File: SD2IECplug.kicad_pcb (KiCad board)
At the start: 2 copper layers, 50 x 49 mm, 39 parts, among them J1 ISP, J2 X6, J4 IEC, J5 C64-CassettePort, J6 C64-CassettePort, J7 Power, J8 X3, Q1 IRLML2803, Q2 IRLML2803, Q3 IRLML2803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

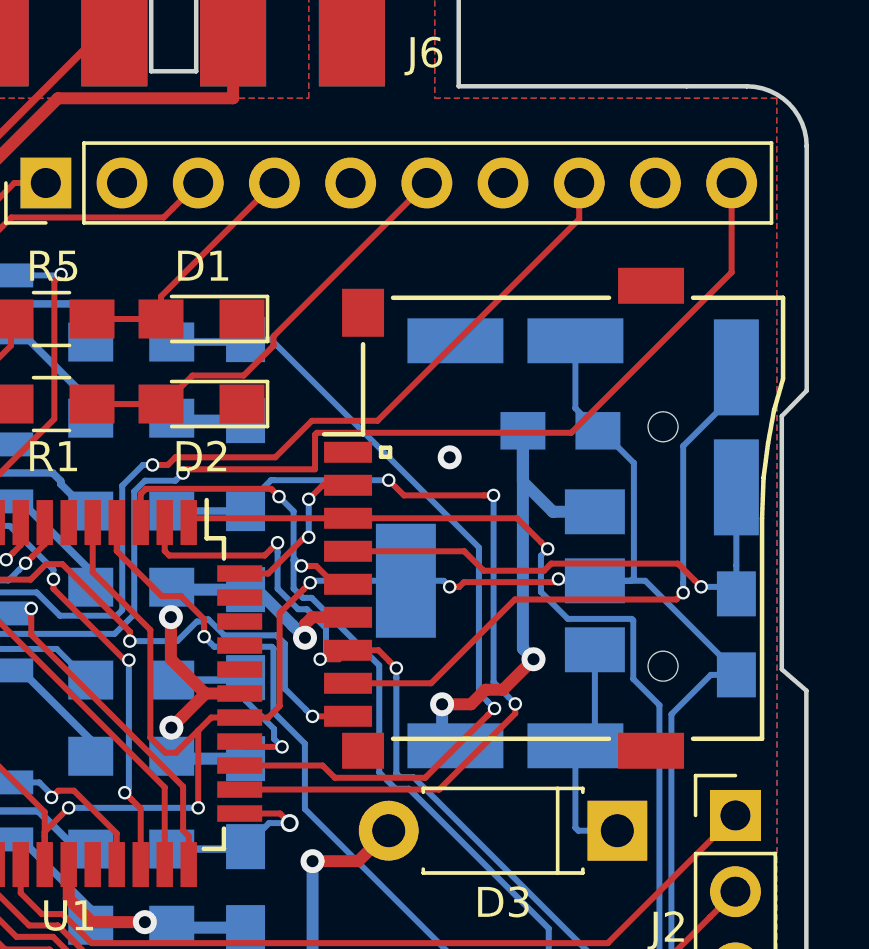
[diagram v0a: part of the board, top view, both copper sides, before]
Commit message: Moced SD connector.
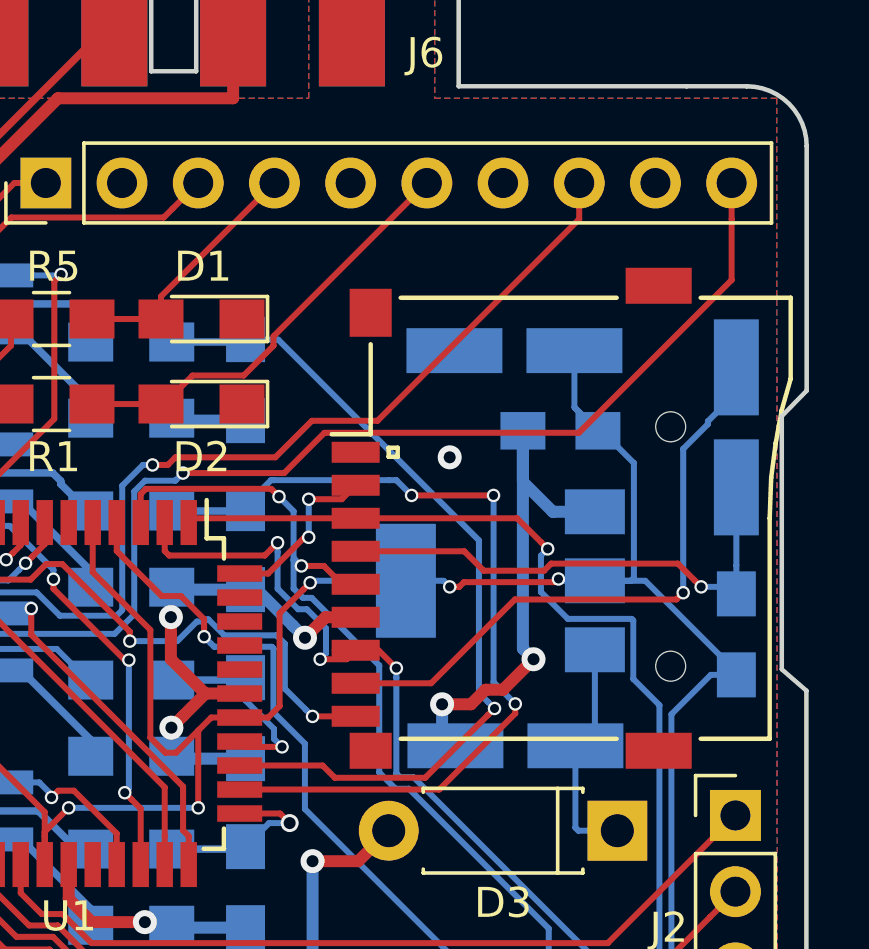
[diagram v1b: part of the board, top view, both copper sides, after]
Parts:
- moved C5 0.33 mm to (98.3, 111.2)
- moved XS1 0.25 mm to (103.5, 116.8)
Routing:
- net +3V3: track 78.6 -> 79.4 mm
- net /IEC_10-11: track 39.0 -> 38.5 mm

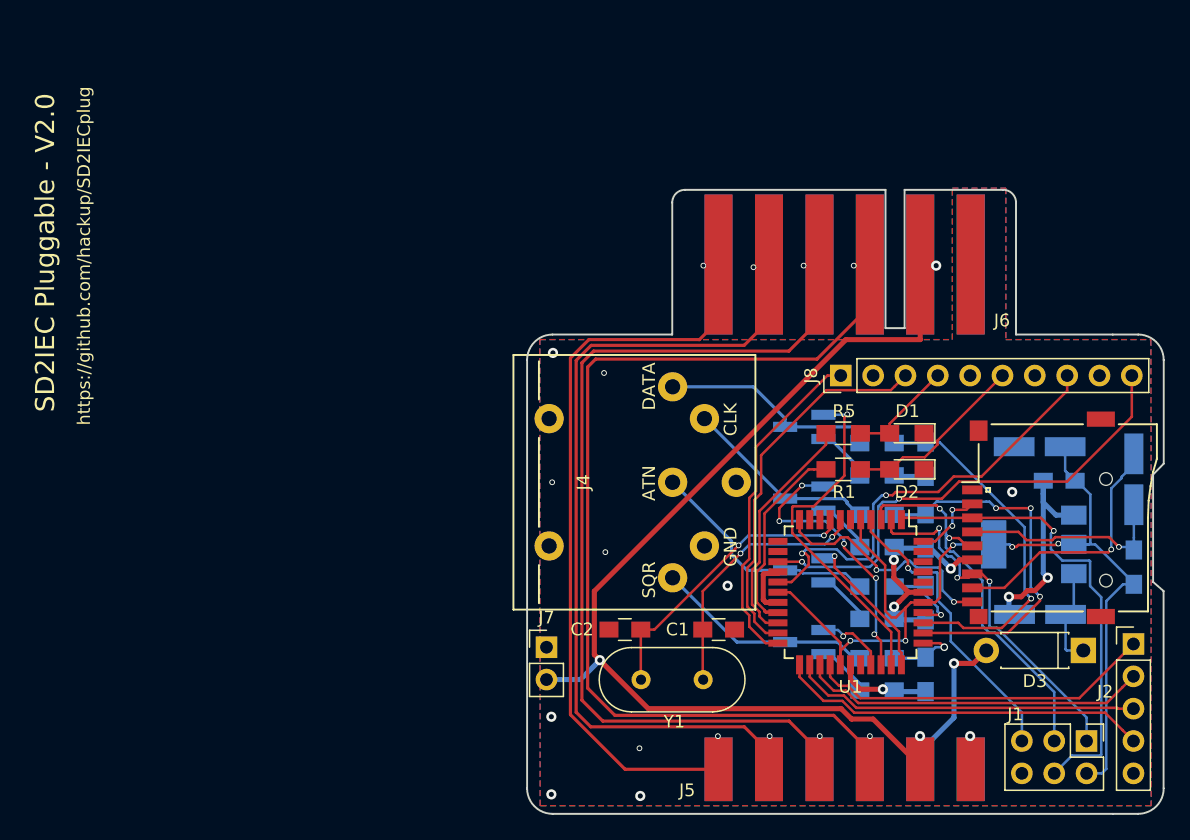
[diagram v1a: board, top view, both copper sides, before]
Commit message: Ziptie holes and silk screen cleanup.
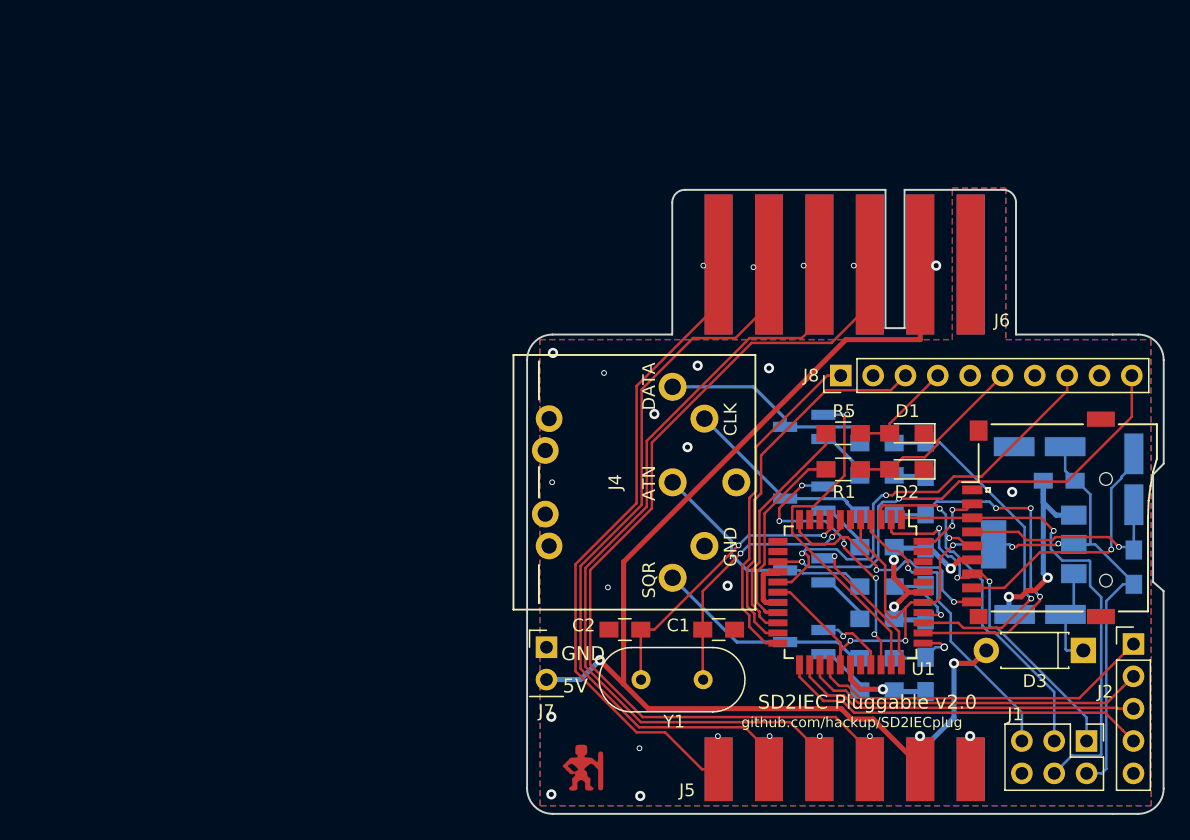
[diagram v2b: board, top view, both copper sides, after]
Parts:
- added G***: LOGO, Logo:bigby2, F.Cu at (62.4, 136.3)
- added MH1: ZipTie, DIN-Connectors:ZipTie_2.7mm, F.Cu at (63.0, 111.6)
- added MH2: ZipTie, DIN-Connectors:ZipTie_2.7mm, F.Cu at (63.0, 116.4)
- J4: footprint DIN-Connectors:DIN-6 -> DIN-Connectors:DIN-6-Variable
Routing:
- net Cas-Read: track 80.4 -> 71.9 mm
- net Cas-Motor: track 86.1 -> 78.2 mm
- net Cas-Sense: track 66.4 -> 58.7 mm
- net Cas-Write: track 74.2 -> 66.6 mm
- net Cas-5V: track 99.1 -> 99.9 mm
- net Cas-GND: vias 17 -> 21
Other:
- board text added: "5V"
- board text added: "SD2IEC Pluggable v2.0"
- board text added: "github.com/hackup/SD2IECplug"
- board text removed: "SD2IEC Pluggable - V2.0"
- board text removed: "https://github.com/hackup/SD2IECplug"

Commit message: Improved routing.
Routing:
- net +3V3: track 79.4 -> 87.6 mm
- net Net-(R7-Pad2): track 28.5 -> 29.0 mm
- net Cas-GND: track 54.6 -> 55.1 mm, vias 21 -> 23

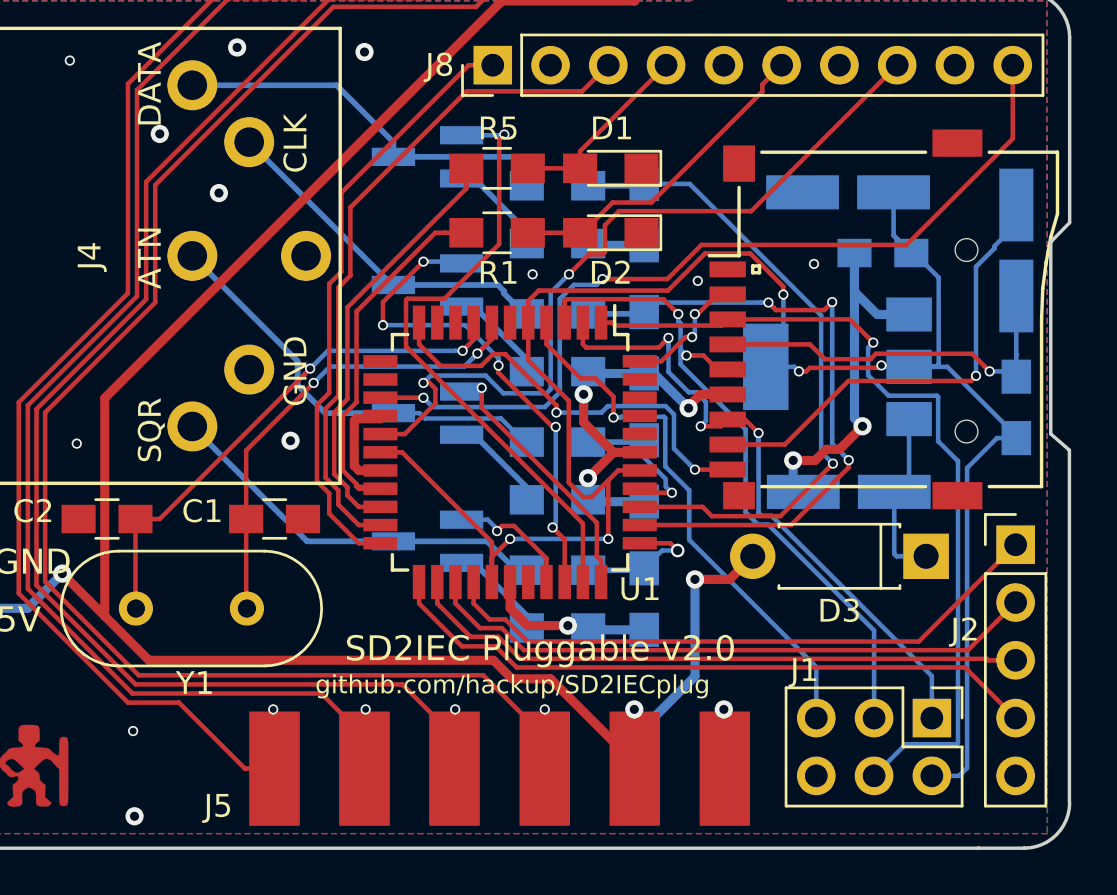
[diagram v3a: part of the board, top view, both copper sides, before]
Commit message: Added missing resistor and yet another breakout header.
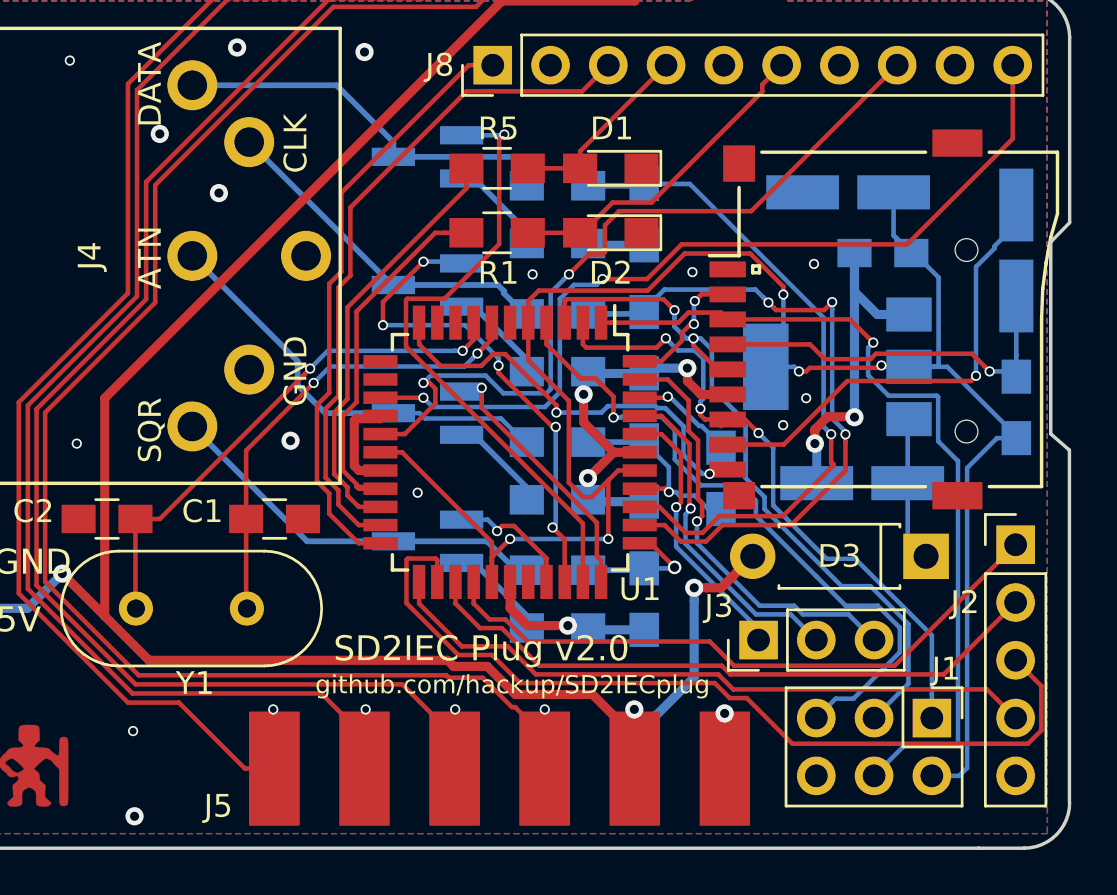
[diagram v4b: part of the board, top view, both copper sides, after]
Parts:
- added J3: Aux, Pin_Headers:Pin_Header_Straight_1x03_Pitch2.54mm, F.Cu at (94.3, 130.9)
- added R16: nB, Resistors_SMD:R_0805_HandSoldering, B.Cu at (92.7, 123.7)
- moved C4 0.70 mm to (98.9, 124.0)
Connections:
- J4 pad 6: (no net) -> Net-(J4-Pad6)
- U1 pad 10: (no net) -> Net-(U1-Pad10)
- U1 pad 12: (no net) -> Net-(U1-Pad12)
- U1 pad 13: (no net) -> Net-(U1-Pad13)
- U1 pad 29: (no net) -> Net-(U1-Pad29)
- U1 pad 40: (no net) -> Net-(J3-Pad1)
- U1 pad 41: (no net) -> Net-(J3-Pad2)
- U1 pad 42: (no net) -> Net-(R16-Pad2)
- U1 pad 43: (no net) -> Net-(J3-Pad3)
- U1 pad 9: (no net) -> Net-(U1-Pad9)
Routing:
- net Net-(J3-Pad3): track 0.00 -> 18.7 mm, vias 0 -> 1
- net Net-(J3-Pad2): track 0.00 -> 14.7 mm, vias 0 -> 1
- net Net-(J3-Pad1): track 0.00 -> 11.9 mm, vias 0 -> 1
- net Net-(J2-Pad3): track 27.4 -> 38.5 mm
- net Net-(J1-Pad5): track 24.0 -> 29.3 mm
- net Net-(R16-Pad2): track 0.00 -> 4.58 mm, vias 0 -> 1
- net Net-(R16-Pad1): track 6.79 -> 9.16 mm
- net SCK: track 30.6 -> 32.5 mm
- net Cas-GND: track 55.1 -> 53.9 mm, vias 23 -> 26
- net Net-(R10-Pad2): track 29.1 -> 30.0 mm
- net Net-(J2-Pad2): track 27.3 -> 28.2 mm
- net Net-(J2-Pad1): track 27.2 -> 28.1 mm
- net Net-(R7-Pad2): track 29.0 -> 29.8 mm
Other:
- board text added: "SD2IEC Plug v2.0"
- board text removed: "SD2IEC Pluggable v2.0"

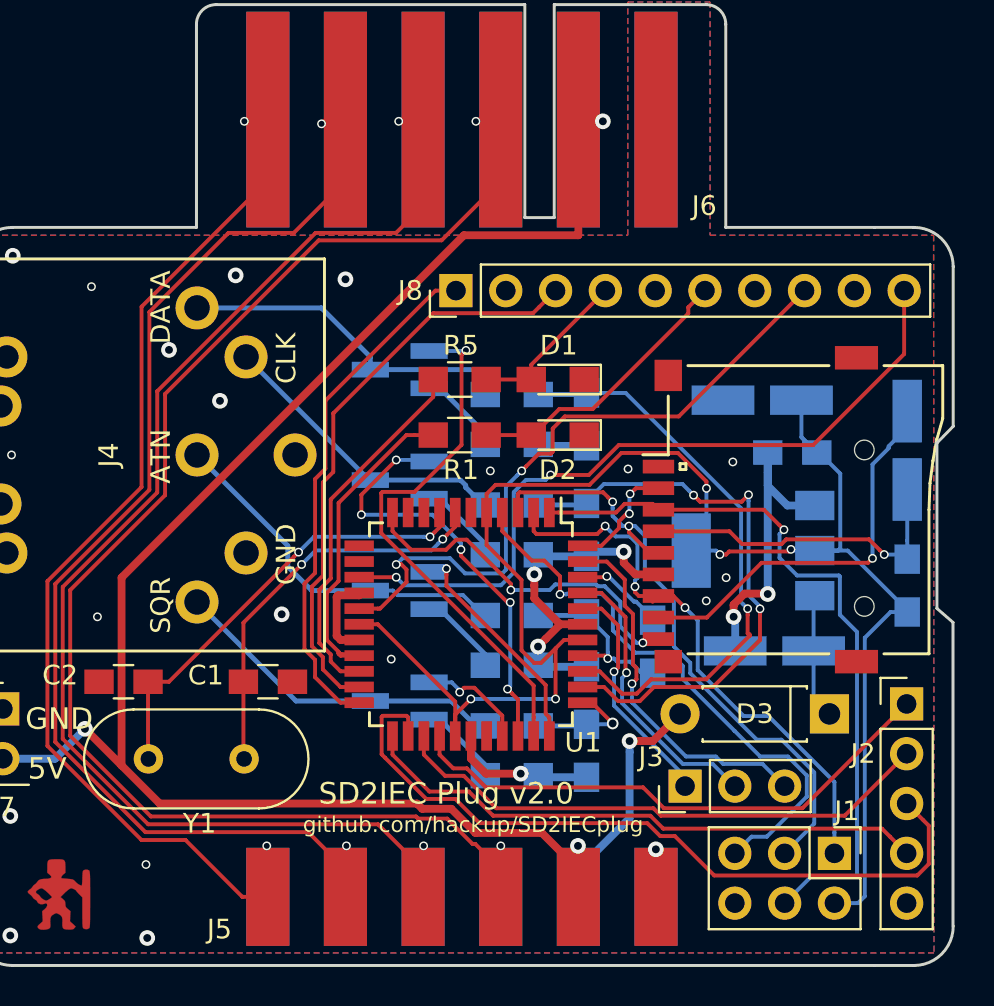
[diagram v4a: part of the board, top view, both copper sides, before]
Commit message: Aligned connectors to grid.
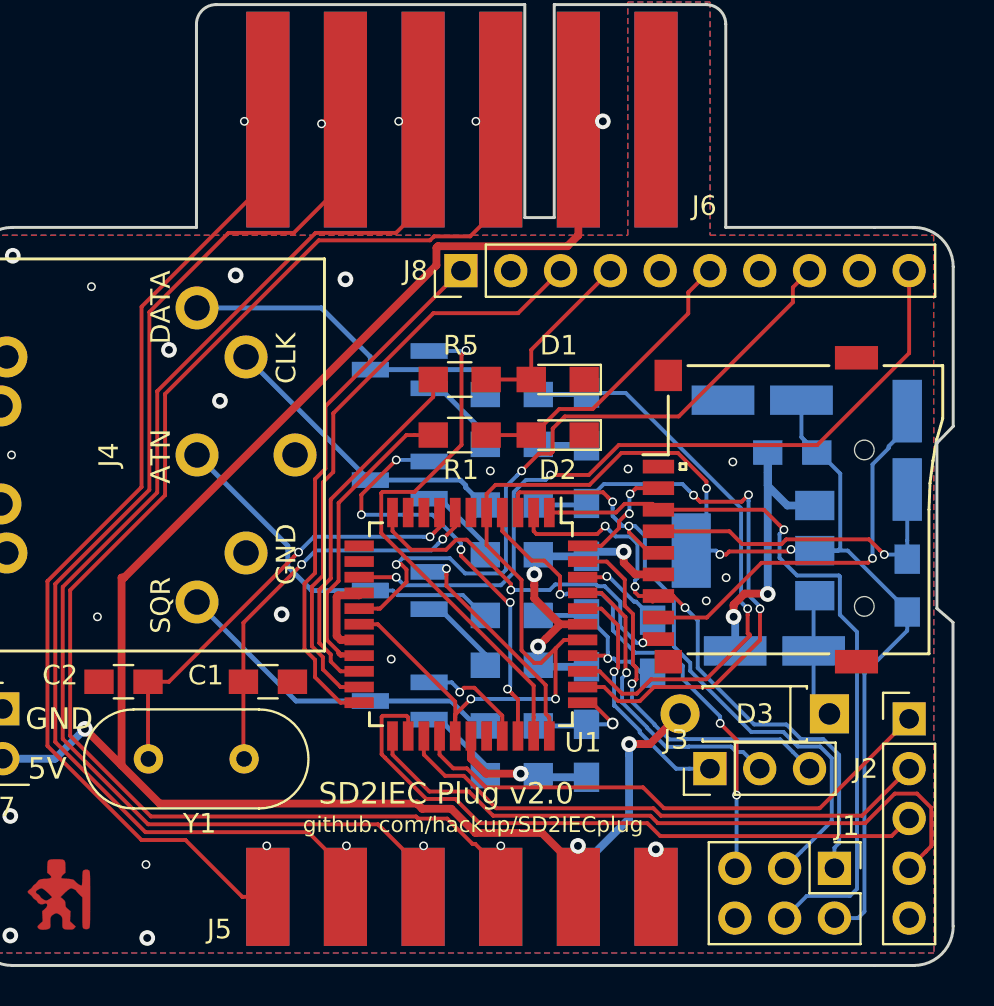
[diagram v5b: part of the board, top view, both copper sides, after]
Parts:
- moved J3 1.55 mm to (95.6, 130.0)
- moved J8 1.05 mm to (82.9, 104.6)
- moved J2 0.77 mm to (105.8, 127.4)
- moved J1 0.76 mm to (101.9, 135.0)
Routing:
- net Net-(J2-Pad4): track 29.3 -> 34.4 mm
- net Net-(J2-Pad3): track 38.5 -> 34.5 mm
- net Net-(J1-Pad5): track 29.3 -> 25.8 mm, vias 1 -> 3
- net SCK: track 32.5 -> 34.9 mm
- net MISO: track 29.5 -> 31.4 mm
- net /IEC_10-11: track 38.5 -> 39.7 mm
- net /LED2: track 14.4 -> 15.5 mm
- net /LED1: track 8.40 -> 9.52 mm
- net /IEC_8-9: track 34.7 -> 35.8 mm
- net Net-(J3-Pad2): track 14.7 -> 15.6 mm
- net Net-(J3-Pad3): track 18.7 -> 19.6 mm
- net MOSI: track 37.8 -> 38.6 mm
- net Cas-Motor: track 78.2 -> 78.9 mm
- net /RESERVE: track 29.9 -> 30.6 mm
- net Net-(J3-Pad1): track 11.9 -> 12.6 mm
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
